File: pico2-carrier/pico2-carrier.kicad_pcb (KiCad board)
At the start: 4 copper layers, 75 x 75 mm, 52 parts, among them IC1 TFDU4101-TT3, IC2 M95512-DWDW4TP_K, IC3 W25Q128JVSIM_TR, IC4 BQ25628ERYKR, J2 DO0180FMST08, J3 Ext_Pwr_Rail, Q1 DMG2305UX-7, SW1 RUN, SW2 BUT_L, SW3 BUT_M, SW4 BUT_R, U1 Pico 2

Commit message: carrier: add helper drawings to pcb
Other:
- board text added: "AMOLED Area"
- board text added: "Mounting holes"
- board text added: "Original PCB"

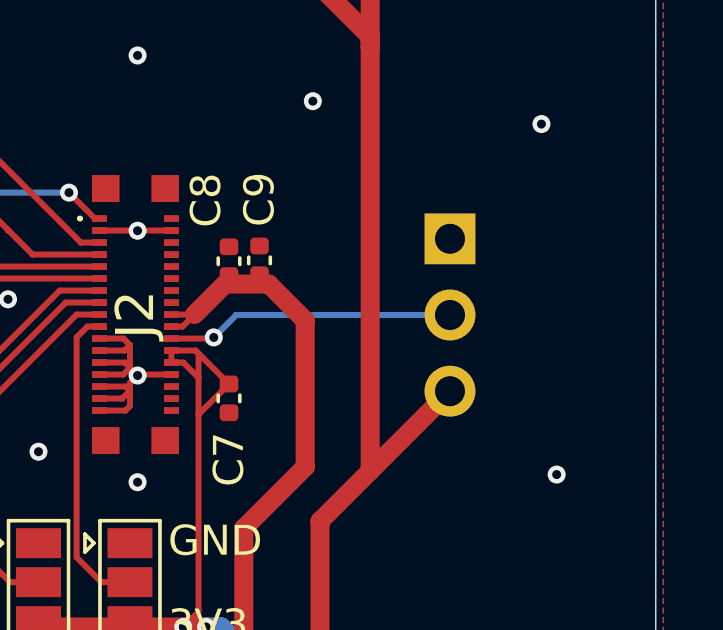
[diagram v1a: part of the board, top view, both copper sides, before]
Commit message: carrier: add some test points and default jumper connections
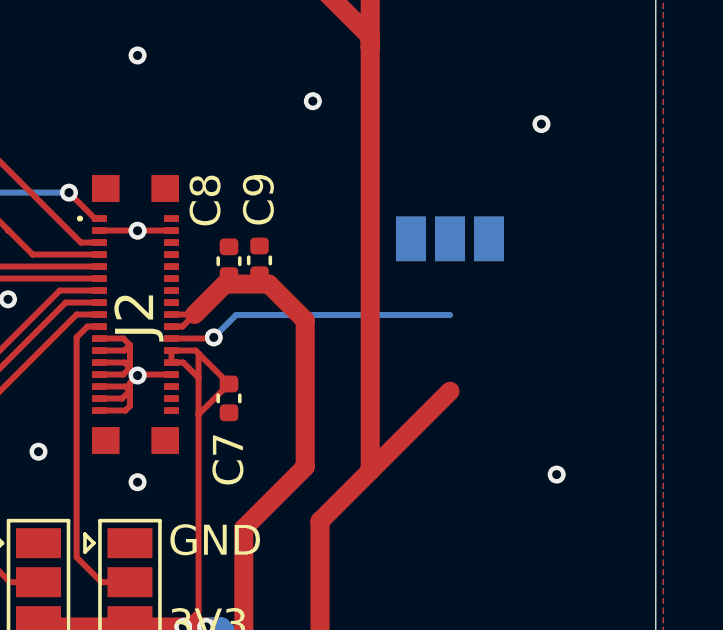
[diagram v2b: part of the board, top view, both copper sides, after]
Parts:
- C11: value 20uF -> 10uF
- JP7: footprint Connector_PinHeader_2.54mm:PinHeader_1x03_P2.54mm_Vertical -> Jumper:SolderJumper-3_P1.3mm_Open_Pad1.0x1.5mm
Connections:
- IC4 pad 7: unconnected-(IC4-~{QON}-Pad7) -> /battery-bq25628e/~{QON}
- J2 pad 10: /screen-headers/TP_SDA -> unconnected-(J2-TP_SDA-Pad10)
- J2 pad 12: /screen-headers/TP_INT -> unconnected-(J2-TP_INT-Pad12)
- J2 pad 14: /screen-headers/TP_RST -> unconnected-(J2-TP_RESET-Pad14)
- J2 pad 16: /screen-headers/TP_VCC -> unconnected-(J2-TP_VCC-Pad16)
- J2 pad 2: /screen-headers/TE -> unconnected-(J2-TE-Pad2)
- J2 pad 34: /screen-headers/VPP -> unconnected-(J2-VPP-Pad34)
- J2 pad 8: /screen-headers/TP_SCL -> unconnected-(J2-TP_SCL-Pad8)
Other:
- board text added: "BAT+"
- board text added: "BAT-"
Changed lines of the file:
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@@
 	(net 33 "/battery-bq25628e/TS_BIAS")
 	(net 34 "/battery-bq25628e/ILIM")
-	(net 35 "unconnected-(IC4-~{QON}-Pad7)")
+	(net 35 "/battery-bq25628e/~{QON}")
 	(net 36 "/I2C_SCL")
 	(net 37 "/battery-bq25628e/TS")
@@
 	(net 46 "/HSTX_SD3")
 	(net 47 "/~{SCREEN_CSB}")
-	(net 48 "/screen-headers/VPP")
-	(net 49 "/screen-headers/TP_SCL")
+	(net 48 "unconnected-(J2-VPP-Pad34)")
+	(net 49 "unconnected-(J2-TP_SCL-Pad8)")
 	(net 50 "unconnected-(J2-NC-Pad6)")
 	(net 51 "unconnected-(J2-MP4-Pad38)")
-	(net 52 "/screen-headers/TP_INT")
+	(net 52 "unconnected-(J2-TP_INT-Pad12)")
 	(net 53 "/screen-headers/IM1")
 	(net 54 "unconnected-(J2-NC-Pad32)")
 	(net 55 "/screen-headers/IM0")
 	(net 56 "unconnected-(J2-MP2-Pad36)")
-	(net 57 "/screen-headers/TP_VCC")
-	(net 58 "/screen-headers/TP_SDA")
-	(net 59 "/screen-headers/TP_RST")
+	(net 57 "unconnected-(J2-TP_VCC-Pad16)")
+	(net 58 "unconnected-(J2-TP_SDA-Pad10)")
+	(net 59 "unconnected-(J2-TP_RESET-Pad14)")
 	(net 60 "unconnected-(J2-NC-Pad30)")
 	(net 61 "unconnected-(J2-MP3-Pad37)")
 	(net 62 "unconnected-(J2-MP1-Pad35)")
-	(net 63 "/screen-headers/TE")
+	(net 63 "unconnected-(J2-TE-Pad2)")
 	(net 64 "/VBUS_OUT")
 	(net 65 "VSYS")
@@
 			)
 		)
-		(property "Value" "20uF"
+		(property "Value" "10uF"
 			(at 0 1.16 0)
 			(layer "F.Fab")
@@
 			(size 0.2 0.6)
 			(layers "F.Cu" "F.Paste" "F.Mask")
-			(net 35 "unconnected-(IC4-~{QON}-Pad7)")
+			(net 35 "/battery-bq25628e/~{QON}")
 			(pinfunction "~{QON}")
-			(pintype "passive+no_connect")
+			(pintype "passive")
 		)
 		(pad "8" smd rect
@@
 			(size 0.23 0.5)
 			(layers "F.Cu" "F.Paste" "F.Mask")
-			(net 63 "/screen-headers/TE")
+			(net 63 "unconnected-(J2-TE-Pad2)")
 			(pinfunction "TE")
 			(pintype "passive+no_connect")
@@
 			(size 0.23 0.5)
 			(layers "F.Cu" "F.Paste" "F.Mask")
-			(net 49 "/screen-headers/TP_SCL")
+			(net 49 "unconnected-(J2-TP_SCL-Pad8)")
 			(pinfunction "TP_SCL")
 			(pintype "passive+no_connect")
@@
 			(size 0.23 0.5)
 			(layers "F.Cu" "F.Paste" "F.Mask")
-			(net 58 "/screen-headers/TP_SDA")
+			(net 58 "unconnected-(J2-TP_SDA-Pad10)")
 			(pinfunction "TP_SDA")
 			(pintype "passive+no_connect")
@@
 			(size 0.23 0.5)
 			(layers "F.Cu" "F.Paste" "F.Mask")
-			(net 52 "/screen-headers/TP_INT")
+			(net 52 "unconnected-(J2-TP_INT-Pad12)")
 			(pinfunction "TP_INT")
 			(pintype "passive+no_connect")
@@
 			(size 0.23 0.5)
 			(layers "F.Cu" "F.Paste" "F.Mask")
-			(net 59 "/screen-headers/TP_RST")
+			(net 59 "unconnected-(J2-TP_RESET-Pad14)")
 			(pinfunction "TP_RESET")
 			(pintype "passive+no_connect")
@@
 			(size 0.23 0.5)
 			(layers "F.Cu" "F.Paste" "F.Mask")
-			(net 57 "/screen-headers/TP_VCC")
+			(net 57 "unconnected-(J2-TP_VCC-Pad16)")
 			(pinfunction "TP_VCC")
 			(pintype "passive+no_connect")
@@
 			(size 0.23 0.5)
 			(layers "F.Cu" "F.Paste" "F.Mask")
-			(net 48 "/screen-headers/VPP")
+			(net 48 "unconnected-(J2-VPP-Pad34)")
 			(pinfunction "VPP")
 			(pintype "passive+no_connect")
@@
 		)
 	)
-	(footprint "Connector_PinHeader_2.54mm:PinHeader_1x03_P2.54mm_Vertical"
+	(footprint "Jumper:SolderJumper-3_P1.3mm_Open_Pad1.0x1.5mm"
 		(layer "B.Cu")
 		(at 183.642 98.983 180)
-		(descr "Through hole straight pin header, 1x03, 2.54mm pitch, single row")
-		(tags "Through hole pin header THT 1x03 2.54mm single row")
+		(descr "SMD Solder 3-pad Jumper, 1x1.5mm Pads, 0.3mm gap, open")
+		(tags "solder jumper open")
 		(property "Reference" "JP7"
-			(at 0 2.33 0)
+			(at 0 1.8 0)
 			(layer "B.SilkS")
 			(effects
@@
 		)
 		(property "Value" "PWR_EN"
-			(at 0 -7.41 0)
+			(at 0 -2 0)
 			(layer "B.Fab")
 			(effects
@@
 			)
 		)
-		(property "Footprint" "Connector_PinHeader_2.54mm:PinHeader_1x03_P2.54mm_Vertical"
+		(property "Footprint" "Jumper:SolderJumper-3_P1.3mm_Open_Pad1.0x1.5mm"
 			(at 0 0 0)
 			(unlocked yes)
@@
 		(sheetname "screen-headers")
 		(sheetfile "screen-headers.kicad_sch")
-		(attr through_hole exclude_from_bom)
+		(zone_connect 1)
+		(attr exclude_from_pos_files exclude_from_bom)
 		(fp_line
-			(start 1.33 -1.27)
-			(end -1.33 -1.27)
+			(start 2.05 1)
+			(end -2.05 1)
 			(stroke
 				(width 0.12)
@@
 		)
 		(fp_line
-			(start 1.33 -6.41)
-			(end 1.33 -1.27)
+			(start 2.05 -1)
+			(end 2.05 1)
 			(stroke
 				(width 0.12)
@@
 		)
 		(fp_line
-			(start 1.33 -6.41)
-			(end -1.33 -6.41)
+			(start -1 -1.5)
+			(end -1.3 -1.2)
 			(stroke
 				(width 0.12)
@@
 		)
 		(fp_line
-			(start 0 1.33)
-			(end -1.33 1.33)
+			(start -1 -1.5)
+			(end -1.6 -1.5)
 			(stroke
 				(width 0.12)
@@
 		)
 		(fp_line
-			(start -1.33 1.33)
-			(end -1.33 0)
+			(start -1.6 -1.5)
+			(end -1.3 -1.2)
 			(stroke
 				(width 0.12)
@@
 		)
 		(fp_line
-			(start -1.33 -6.41)
-			(end -1.33 -1.27)
+			(start -2.05 1)
+			(end -2.05 -1)
 			(stroke
 				(width 0.12)
@@
 		)
 		(fp_line
-			(start 1.8 1.8)
-			(end 1.8 -6.85)
+			(start -2.05 -1)
+			(end 2.05 -1)
 			(stroke
-				(width 0.05)
+				(width 0.12)
 				(type solid)
 			)
-			(layer "B.CrtYd")
+			(layer "B.SilkS")
 		)
 		(fp_line
-			(start 1.8 -6.85)
-			(end -1.8 -6.85)
+			(start 2.3 1.25)
+			(end 2.3 -1.25)
 			(stroke
 				(width 0.05)
@@
 		)
 		(fp_line
-			(start -1.8 1.8)
-			(end 1.8 1.8)
+			(start 2.3 1.25)
+			(end -2.3 1.25)
 			(stroke
 				(width 0.05)
@@
 		)
 		(fp_line
-			(start -1.8 -6.85)
-			(end -1.8 1.8)
+			(start -2.3 -1.25)
+			(end 2.3 -1.25)
 			(stroke
 				(width 0.05)
@@
 		)
 		(fp_line
-			(start 1.27 1.27)
-			(end -0.635 1.27)
-			(stroke
-				(width 0.1)
-				(type solid)
-			)
-			(layer "B.Fab")
-		)
-		(fp_line
-			(start 1.27 -6.35)
-			(end 1.27 1.27)
-			(stroke
-				(width 0.1)
-				(type solid)
-			)
-			(layer "B.Fab")
-		)
-		(fp_line
-			(start -0.635 1.27)
-			(end -1.27 0.635)
-			(stroke
-				(width 0.1)
-				(type solid)
-			)
-			(layer "B.Fab")
-		)
-		(fp_line
-			(start -1.27 0.635)
-			(end -1.27 -6.35)
-			(stroke
-				(width 0.1)
-				(type solid)
-			)
-			(layer "B.Fab")
-		)
-		(fp_line
-			(start -1.27 -6.35)
-			(end 1.27 -6.35)
+			(start -2.3 -1.25)
+			(end -2.3 1.25)
 			(stroke
-				(width 0.1)
+				(width 0.05)
 				(type solid)
 			)
-			(layer "B.Fab")
-		)
-		(fp_text user "${REFERENCE}"
-			(at 0 -2.54 90)
-			(layer "B.Fab")
-			(effects
-				(font
-					(size 1 1)
-					(thickness 0.15)
-				)
-				(justify mirror)
-			)
+			(layer "B.CrtYd")
 		)
-		(pad "1" thru_hole rect
-			(at 0 0 180)
-			(size 1.7 1.7)
-			(drill 1)
-			(layers "*.Cu" "*.Mask")
-			(remove_unused_layers no)
+		(pad "1" smd rect
+			(at -1.3 0 180)
+			(size 1 1.5)
+			(layers "B.Cu" "B.Mask")
 			(net 4 "GND")
 			(pinfunction "A")
 			(pintype "passive")
 		)
-		(pad "2" thru_hole oval
-			(at 0 -2.54 180)
-			(size 1.7 1.7)
-			(drill 1)
-			(layers "*.Cu" "*.Mask")
-			(remove_unused_layers no)
+		(pad "2" smd rect
+			(at 0 0 180)
+			(size 1 1.5)
+			(layers "B.Cu" "B.Mask")
 			(net 45 "/screen-headers/PWR_EN")
 			(pinfunction "C")
 			(pintype "passive")
 		)
-		(pad "3" thru_hole oval
-			(at 0 -5.08 180)
-			(size 1.7 1.7)
-			(drill 1)
-			(layers "*.Cu" "*.Mask")
-			(remove_unused_layers no)
+		(pad "3" smd rect
+			(at 1.3 0 180)
+			(size 1 1.5)
+			(layers "B.Cu" "B.Mask")
 			(net 6 "+3.3V")
 			(pinfunction "B")
 			(pintype "passive")
 		)
-		(model "${KICAD8_3DMODEL_DIR}/Connector_PinHeader_2.54mm.3dshapes/PinHeader_1x03_P2.54mm_Vertical.wrl"
-			(offset
-				(xyz 0 0 0)
-			)
-			(scale
-				(xyz 1 1 1)
-			)
-			(rotate
-				(xyz 0 0 0)
-			)
-		)
 	)
 	(footprint "Connector_PinHeader_2.54mm:PinHeader_1x02_P2.54mm_Vertical"
@@
 	)
 	(gr_rect
-		(start 207 21.1)
-		(end 245 51.7)
+		(start 134 84.6)
+		(end 172 115.2)
 		(stroke
 			(width 0.1)
@@
 		)
 	)
+	(gr_text "BAT+"
+		(at 133.546 136.446 0)
+		(layer "B.SilkS")
+		(effects
+			(font
+				(size 1 1)
+				(thickness 0.1)
+			)
+			(justify left bottom mirror)
+		)
+	)
 	(gr_text "VBUS"
 		(at 117.856 120.558 90)
 		(layer "B.SilkS")
 		(effects
+			(font
+				(size 1 1)
+				(thickness 0.1)
+			)
+			(justify left bottom mirror)
+		)
+	)
+	(gr_text "BAT-"
+		(at 144.5 137.6 0)
+		(layer "B.SilkS")
+		(effects

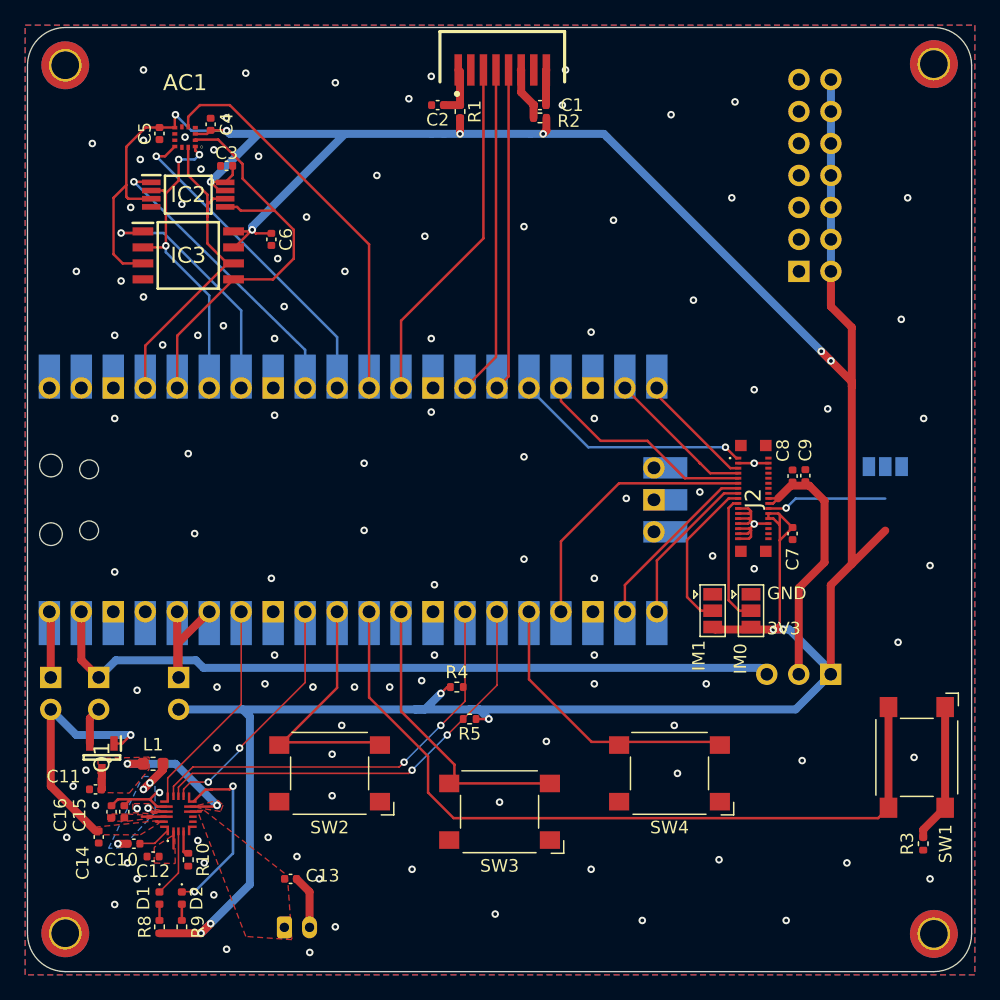
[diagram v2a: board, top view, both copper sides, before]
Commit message: carrier: small pcb updates
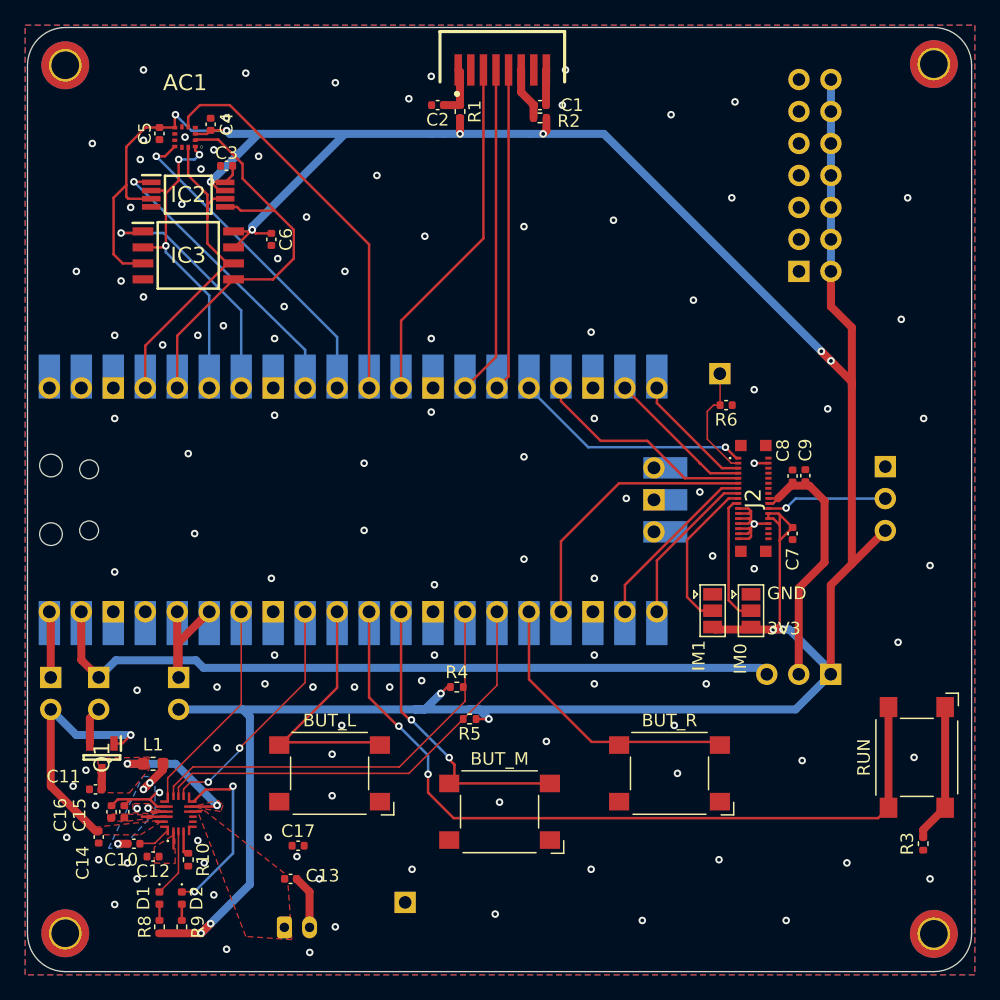
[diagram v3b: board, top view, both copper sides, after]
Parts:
- added C17: 10uF, Capacitor_SMD:C_0402_1005Metric, F.Cu at (137.0, 129.1)
- added R6: 0R, Capacitor_SMD:C_0402_1005Metric, F.Cu at (171.0, 94.1)
- added TP1: ~{QON}, Connector_PinHeader_2.54mm:PinHeader_1x01_P2.54mm_Vertical, B.Cu at (145.5, 133.6)
- added TP2: DCX_RS, Connector_PinHeader_2.54mm:PinHeader_1x01_P2.54mm_Vertical, B.Cu at (170.5, 91.6)
- C14: value 1uF -> 10uF
- JP7: footprint Jumper:SolderJumper-3_P1.3mm_Open_Pad1.0x1.5mm -> Connector_PinHeader_2.54mm:PinHeader_1x03_P2.54mm_Vertical
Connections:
- J2 pad 3: GND -> /screen-headers/DCX_RS
- JP5 pad 1: GND -> +3.3V
- JP5 pad 3: +3.3V -> GND
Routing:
- net /screen-headers/DCX_RS: track 0.00 -> 9.37 mm
- net GND: track 27.1 -> 25.8 mm
- net /BUT_M: track 23.4 -> 23.8 mm, vias 0 -> 2
- net /RUN: track 62.1 -> 62.2 mm, vias 0 -> 2
- net /I2C_SCL: vias 2 -> 0
- net /I2C_SDA: vias 2 -> 0
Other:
- board text removed: "Ext. Power"
- board text removed: "SCREEN_PWR_EN"
- board text removed: "SCREEN_PWR_SRC"

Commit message: carrier: add 3.3V zone, start tidying buttons, update caps to 0603
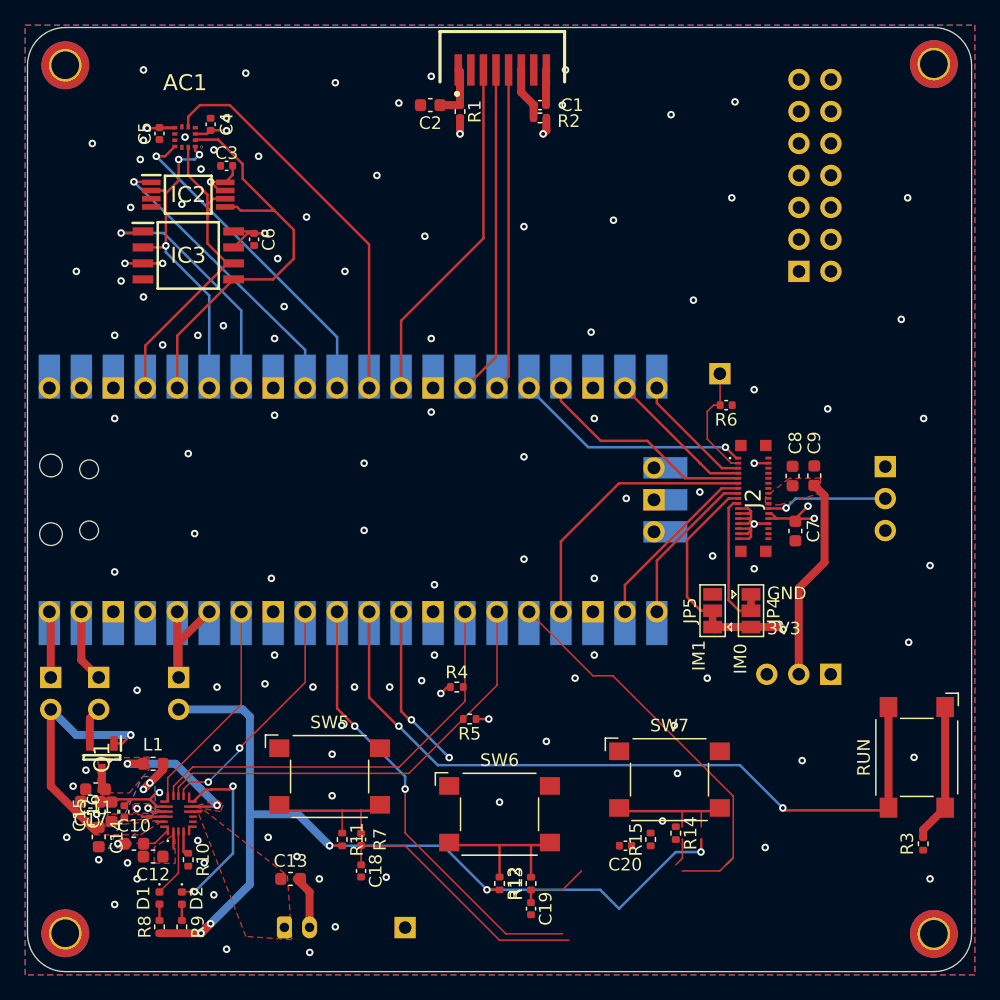
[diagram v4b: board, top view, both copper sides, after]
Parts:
- removed SW2: BUT_L, Button_Switch_SMD:SW_SPST_Omron_B3FS-101xP
- removed SW3: BUT_M, Button_Switch_SMD:SW_SPST_Omron_B3FS-101xP
- removed SW4: BUT_R, Button_Switch_SMD:SW_SPST_Omron_B3FS-101xP
- added C18: 0.1uF, Capacitor_SMD:C_0402_1005Metric, F.Cu at (142.0, 131.1)
- added C19: 0.1uF, Capacitor_SMD:C_0402_1005Metric, F.Cu at (155.5, 134.1)
- added C20: 0.1uF, Capacitor_SMD:C_0402_1005Metric, F.Cu at (163.0, 129.1)
- added R11: 10k, Resistor_SMD:R_0402_1005Metric, F.Cu at (140.5, 128.6)
- added R12: 10k, Resistor_SMD:R_0402_1005Metric, F.Cu at (153.0, 132.1)
- added R13: 1k, Resistor_SMD:R_0402_1005Metric, F.Cu at (155.5, 132.1)
- added R14: 10k, Resistor_SMD:R_0402_1005Metric, F.Cu at (167.0, 128.1)
- added R15: 1k, Resistor_SMD:R_0402_1005Metric, F.Cu at (165.0, 128.6)
- added R7: 1k, Capacitor_SMD:C_0402_1005Metric, F.Cu at (142.0, 128.6)
- added SW5: BUT_L, Button_Switch_SMD:SW_SPST_Omron_B3FS-101xP, F.Cu at (139.5, 123.6)
- added SW6: BUT_M, Button_Switch_SMD:SW_SPST_Omron_B3FS-101xP, F.Cu at (153.0, 126.6)
- added SW7: BUT_R, Button_Switch_SMD:SW_SPST_Omron_B3FS-101xP, F.Cu at (166.5, 123.8)
- C10, C11, C12, C13, C14, C16, C17, C2, C7, C8, C9: footprint Capacitor_SMD:C_0402_1005Metric -> Capacitor_SMD:C_0603_1608Metric
- JP4, JP5: footprint Jumper:SolderJumper-3_P1.3mm_Open_Pad1.0x1.5mm -> Jumper:SolderJumper-3_P1.3mm_Bridged12_Pad1.0x1.5mm
- moved C17 16.9 mm to (120.5, 125.6), turned to 180 degrees
- moved TP1 2.00 mm to (145.5, 135.6)
- moved C6 1.37 mm to (133.5, 80.9)
- moved C9 0.71 mm to (178.0, 99.7)
- moved C2 0.58 mm to (147.5, 70.3)
- moved C7 0.30 mm to (176.5, 104.1)
- turned JP5 to 90 degrees
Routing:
- net +3.3V: track 276.7 -> 107.6 mm, vias 14 -> 18
- net /VSYS_IN: track 59.9 -> 5.79 mm
- net /BUT_L: track 20.2 -> 57.1 mm, vias 0 -> 2
- net /buttons-debounce/BUT_M_1: track 0.00 -> 13.1 mm
- net /BUT_R: track 23.0 -> 34.7 mm
- net /buttons-debounce/BUT_L_1: track 0.00 -> 11.6 mm
- net /buttons-debounce/BUT_R_1: track 0.00 -> 10.5 mm
- net /screen-headers/SCREEN_VBAT: track 20.8 -> 16.2 mm
- net /BUT_M: track 23.8 -> 19.3 mm
- net /RUN: track 62.2 -> 59.9 mm
- net GND: vias 114 -> 110
- added copper zone on In2.Cu, net +3.3V
- added copper zone on In2.Cu, net /VSYS_IN
- added copper zone on F.Cu, net /screen-headers/SCREEN_VBAT
